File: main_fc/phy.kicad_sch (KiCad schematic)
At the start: 28 parts, among them J7 ARJM11A1-009-AB-EW2, U6 LAN8742A, Y2 25M

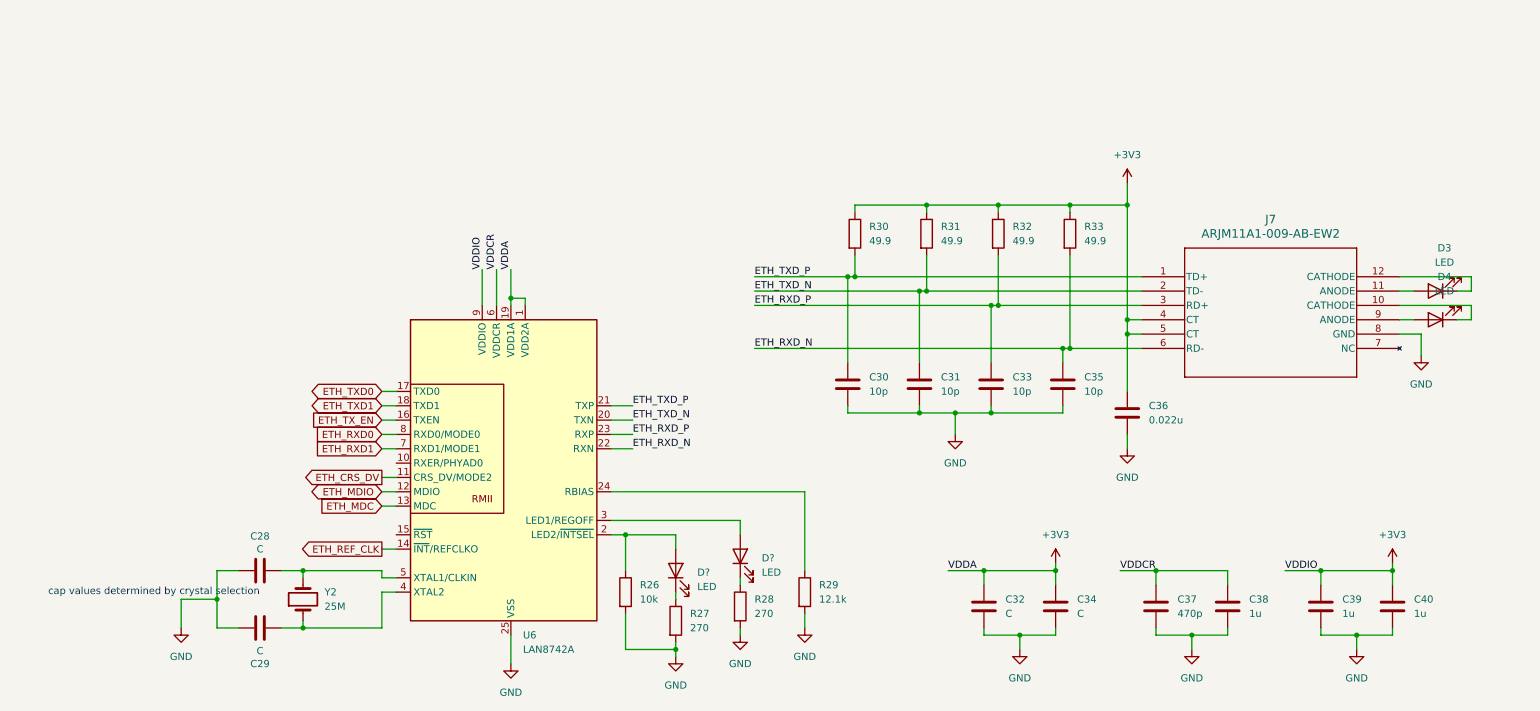
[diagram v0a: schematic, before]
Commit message: main flight computer annotations and passive footprints
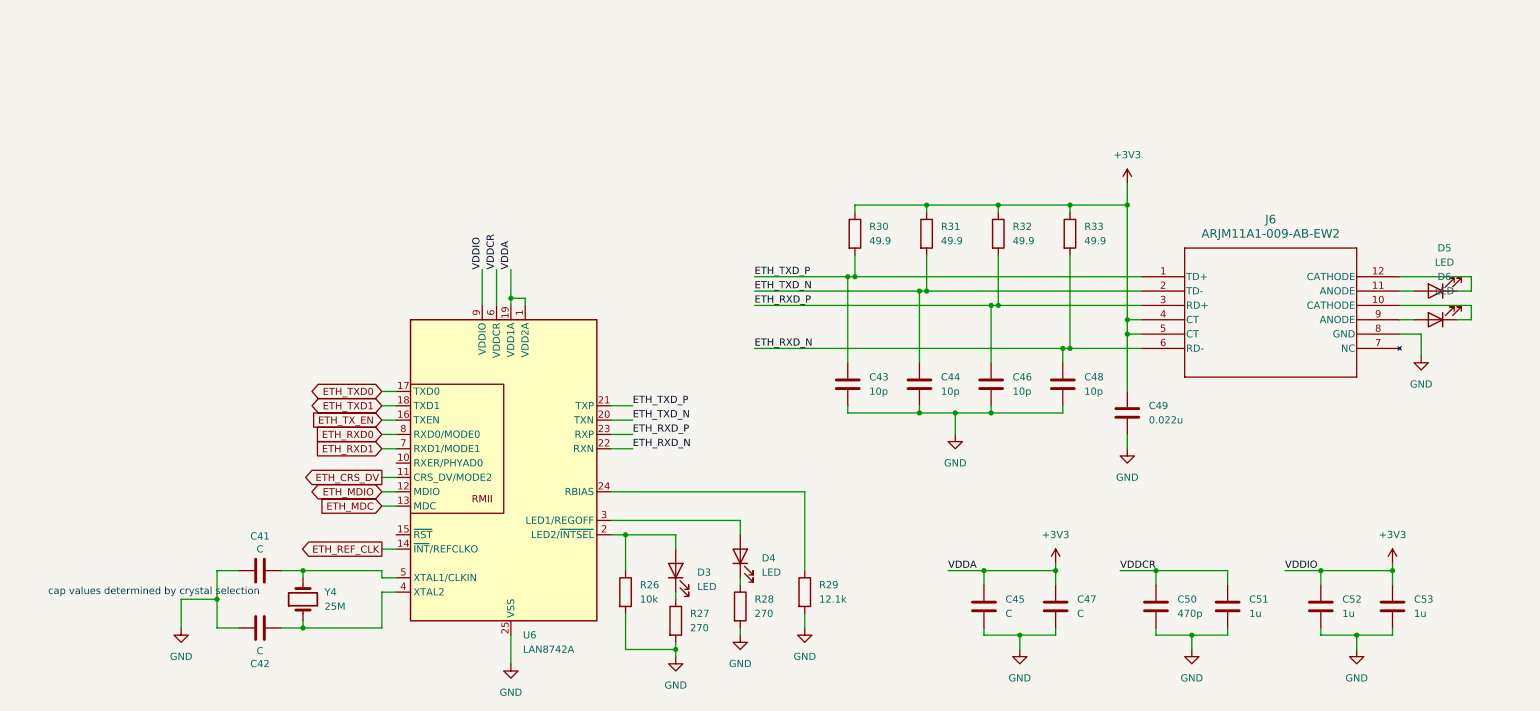
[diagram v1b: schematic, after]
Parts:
- C41: renamed from C28; footprint (none) -> Capacitor_SMD:C_0603_1608Metric
- C42: renamed from C29; footprint (none) -> Capacitor_SMD:C_0603_1608Metric
- C43: renamed from C30; footprint (none) -> Capacitor_SMD:C_0603_1608Metric
- C44: renamed from C31; footprint (none) -> Capacitor_SMD:C_0603_1608Metric
- C45: renamed from C32; footprint (none) -> Capacitor_SMD:C_0603_1608Metric
- C46: renamed from C33; footprint (none) -> Capacitor_SMD:C_0603_1608Metric
- C47: renamed from C34; footprint (none) -> Capacitor_SMD:C_0603_1608Metric
- C48: renamed from C35; footprint (none) -> Capacitor_SMD:C_0603_1608Metric
- C49: renamed from C36; footprint (none) -> Capacitor_SMD:C_0603_1608Metric
- C50: renamed from C37; footprint (none) -> Capacitor_SMD:C_0603_1608Metric
- C51: renamed from C38; footprint (none) -> Capacitor_SMD:C_0603_1608Metric
- C52: renamed from C39; footprint (none) -> Capacitor_SMD:C_0603_1608Metric
- C53: renamed from C40; footprint (none) -> Capacitor_SMD:C_0603_1608Metric
- R26, R27, R28, R29, R30, R31, R32, R33: footprint (none) -> Resistor_SMD:R_0603_1608Metric
- gave numbers to parts that had none: 2
- renumbered D3 to D5, D4 to D6, J7 to J6, Y2 to Y4

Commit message: added new stm symbol/footprint
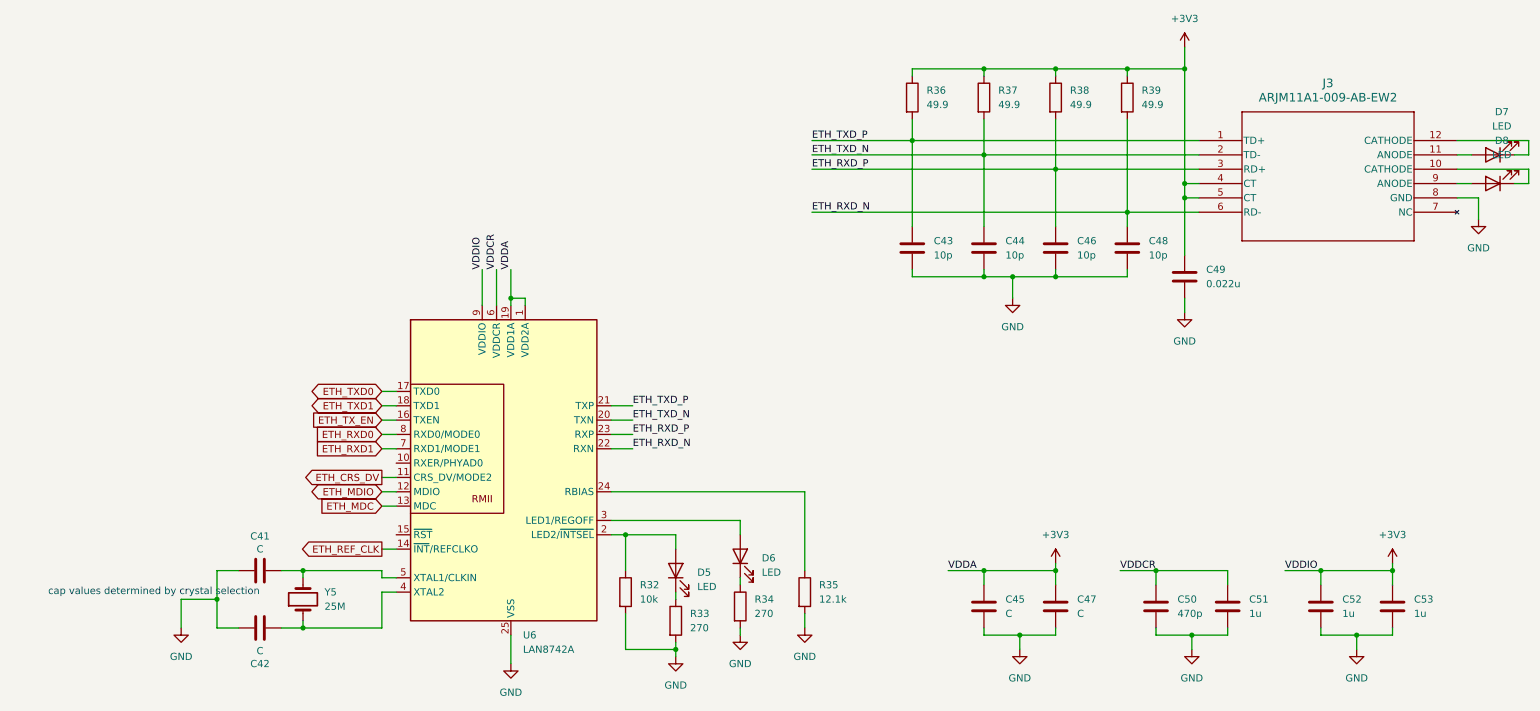
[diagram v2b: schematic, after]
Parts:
- renumbered D3 to D5, D4 to D6, D5 to D7, D6 to D8, J6 to J3, R26 to R32, R27 to R33, R28 to R34, R29 to R35, R30 to R36, R31 to R37, R32 to R38, R33 to R39, Y4 to Y5
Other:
- moved on the sheet: C43, C44, C46, C48, C49, D7, D8, J3, R36, R37, R38, R39
